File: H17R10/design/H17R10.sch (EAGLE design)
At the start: 94 parts, among them P1 HEXABIT__X3_NO_P1_P2_P3_P4_P5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, P4 PAD4, P5 PAD4, P6 PAD4, U1 STM32F091RBT6STMICROELECTRONI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, U2 POWERSTEP01, U3 TEXAS_INSTRUMENTS_ISO7741DBQR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, U4 TEXAS_INSTRUMENTS_ISO7742DBQR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, X1 XTALL_CSTCE8M00G52

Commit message: -Changing the MCU to STM32G0B1CEU6N -Editing the electronic design -Editing the layout design to improve the performance
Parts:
- removed A1, A2, B1, B2, BZY: YELLOW, HEXABITZ_USER_INTERFACE_PARTS:VLMY1300-GS08
- removed B, C, D, R: PAD1, Hexabitz:PAD1
- removed C22: 1.00uF, Hexabitz:C-0805-POL
- removed C23, C24: 4.7uF, Hexabitz:C-0805-POL
- removed C25: 10nF, Hexabitz:C-0603
- removed C26, C27, C28, C29: 100nF, Hexabitz:C-0603
- removed CCW, CW, PWR: Green, HEXABITZ_USER_INTERFACE_PARTS:VLMTG1300-GS08
- removed D0, FLT, S: RED, HEXABITZ_USER_INTERFACE_PARTS:VLMS1300-GS08
- removed EMG_SW, SPI_MTR: 3-644456-2, HEXABITZ_USER_INTERFACE_PARTS:3-644456-2
- removed P1: HEXABIT__X3_NO_P1_P2_P3_P4_P5_P6_P11_P12, hexabitz_connectors:HEXABIT__X3_NO_P1_P2_P3_P4_P5_P6_P11_P12
- removed P4, P5, P6, VCCIO, VCCIO1, VS: PAD4, HEXABITZ_CONNECTION_PARTS:PAD4
- removed R16, R17, R18, R19: 10k, HEXABITZ_RCLS:R-0805
- removed R20, R21: 330, HEXABITZ_RCLS:R-0603
- removed R22, R27, R33, R34: DNP, HEXABITZ_RCLS:R-0603
- removed R23: 0R, HEXABITZ_RCLS:R-0603
- removed R24, R28: DNP, HEXABITZ_RCLS:R-0805
- removed R25, R26: 39K, HEXABITZ_RCLS:R-0603
- removed R31: 270.0R, HEXABITZ_RCLS:R-0603
- removed R32: 10.0K, Hexabitz:R-0603
- removed U3: TEXAS_INSTRUMENTS_ISO7741DBQRTEXAS_INSTRUMENTS_ISO7741DBQR_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, HEXABITZ_ICs:TEXAS_INSTRUMENTS_ISO7741DBQRTEXAS_INSTRUMENTS_ISO7741DBQR_0_0
- removed U4: TEXAS_INSTRUMENTS_ISO7742DBQRTEXAS_INSTRUMENTS_ISO7742DBQR_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, Texas Instruments - ISO7742DBQR:TEXAS_INSTRUMENTS_ISO7742DBQRTEXAS_INSTRUMENTS_ISO7742DBQR_0_3
- added C20: 470nF, HEXABITZ_RCLS:C-0603
- added CK, CS, SDI, SDO: PAD4, HEXABITZ_CONNECTION_PARTS:PAD4
- added D2: STMICROELECTRONICS_BAT46ZFILMSTMICROELECTRONICS_BAT46ZFILM_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, HEXABITZ_RCLS:STMICROELECTRONICS_BAT46ZFILMSTMICROELECTRONICS_BAT46ZFILM_0_3
- added D3, D5, D6, D7: YELLOW, HEXABITZ_USER_INTERFACE_PARTS:VLMY1300-GS08
- added D4: STMICROELECTRONICS_BAR43SFILMSTMICROELECTRONICS_BAR43SFILM_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, HEXABITZ_RCLS:STMICROELECTRONICS_BAR43SFILMSTMICROELECTRONICS_BAR43SFILM_0_0
- added D8: RED, HEXABITZ_USER_INTERFACE_PARTS:VLMS1300-GS08
- added FB1: (no value), HEXABITZ_RCLS:FB-TDK_MMZ1608Y300B
- added J1: 3-644456-2, HEXABITZ_USER_INTERFACE_PARTS:3-644456-2
- added JP1: (no value), HEXABITZ_USER_INTERFACE_PARTS:PINHD-1X1
- added JP2: (no value), pinhead:PINHD-1X3
- added R12: 330, HEXABITZ_RCLS:R-0603
- added SJ1, SJ2: (no value), jumper:SJW
- added U$1: HEXABIT_17.32_X3_NO_P1_P2_P3_P4_P5_P6_P11_P12, hexabitz_connectors:HEXABIT_17.32_X3_NO_P1_P2_P3_P4_P5_P6_P11_P12
- C1: MFN TDK CORPORATION -> AVX CORPORATION; MPN C1608X7R1H104K080AA -> 0603YC104K4T2A; OCTOPART_URL https://octopart.com/c1608x7r1h104k080aa-tdk-25947665?r=sp -> 'https://octopart.com/0603yc104k4t2a-avx+interconnect+%2F+e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; TOLERANCE (none) -> 10%; VOLTAGE_RATING (none) -> 16.0 V
- C10: value 220nF -> 68uF; device HEXABITZ_RCLS:C-0805 -> HEXABITZ_RCLS:WCAP-ASLI_12.5X14EEVFK2A680Q
- C14: value 68uF -> 220nF; device HEXABITZ_RCLS:WCAP-ASLI_12.5X14EEVFK2A680Q -> HEXABITZ_RCLS:C-0805
- C15: value 68uF -> 47nF; device HEXABITZ_RCLS:WCAP-ASLI_12.5X14EEVFK2A680Q -> HEXABITZ_RCLS:C-0805; MFN (none) -> KEMET; MPN (none) -> C0805C473K1RACTU; OCTOPART_URL (none) -> https://octopart.com/c0805c473k1ractu-kemet-12557765?r=sp; VOLTAGE_RATING (none) -> 100V
- C16, C17, C6: MFN TDK CORPORATION -> AVX CORPORATION; MPN C1608X7R1H104K080AA -> '0603YC104K4T2A; OCTOPART_URL https://octopart.com/c1608x7r1h104k080aa-tdk-25947665?r=sp -> 'https://octopart.com/0603yc104k4t2a-avx+interconnect+%2F+e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; TOLERANCE (none) -> 10%; VOLTAGE_RATING (none) -> 16.0 V
- C18: value 100nF -> 470nF; CAPACITANCE 100nF -> (none); MFN TDK CORPORATION -> TDK; MPN C1608X7R1H104K080AA -> CGA3E3X7R1E474K080AE; OCTOPART_URL https://octopart.com/c1608x7r1h104k080aa-tdk-25947665?r=sp -> https://octopart.com/search?q=CAP+CER+470nF+25V+X7R+0603&cu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; VOLTAGE_RATING (none) -> 100V
- C19: value 100nF -> 220nF; CAPACITANCE 100nF -> (none); MFN TDK CORPORATION -> TDK; MPN C1608X7R1H104K080AA -> CGA3E3X7R1V224K080AE; OCTOPART_URL https://octopart.com/c1608x7r1h104k080aa-tdk-25947665?r=sp -> https://octopart.com/cga3e3x7r1v224k080ae-tdk-68305867?r=sp
- C2: value 220nF -> 100nF; CAPACITANCE (none) -> 100nF; MFN TDK -> AVX CORPORATION; MPN CGA3E3X7R1V224K080AE -> '0603YC104K4T2A; OCTOPART_URL https://octopart.com/cga3e3x7r1v224k080ae-tdk-68305867?r=sp -> 'https://octopart.com/0603yc104k4t2a-avx+interconnect+%2F+e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; TOLERANCE (none) -> 10%; VOLTAGE_RATING (none) -> 16.0 V
- C21: value 100nF -> 22uF; device HEXABITZ_RCLS:C-0603 -> HEXABITZ_RCLS:C-0805-POL; CAPACITANCE 100nF -> (none); MPN C0603C104K8RACTU -> T491A226K006AT; OCTOPART_URL https://octopart.com/c0603c104k8ractu-kemet-145075?r=sp&s=9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 -> https://octopart.com/t491a226k006at-kemet-968601?r=sp; TOLERANCE 10% -> (none); VOLTAGE_RATING 10V -> 6.3V
- C3: value 470nF -> 4.7uF; device HEXABITZ_RCLS:C-0603 -> HEXABITZ_RCLS:C-0805-POL; CAPACITANCE (none) -> 4.7uF; MFN TDK -> 'Panasonic; MPN CGA3E3X7R1E474K080AE -> '10TPU4R7MSI; OCTOPART_URL https://octopart.com/search?q=CAP+CER+470nF+25V+X7R+0603&cu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 -> https://octopart.com/10tpu4r7msi-panasonic-29487748?r=sp; TOLERANCE (none) -> 20%; VOLTAGE_RATING (none) -> 10.0 V
- C4: value 3.3nF -> 100nF; MFN TDK CORPORATION -> AVX CORPORATION; MPN C1608X7R1H104K080AA -> '0603YC104K4T2A; OCTOPART_URL https://octopart.com/c1608x7r1h104k080aa-tdk-25947665?r=sp -> 'https://octopart.com/0603yc104k4t2a-avx+interconnect+%2F+e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; TOLERANCE (none) -> 10%; VOLTAGE_RATING (none) -> 16.0 V
- C5: value DNP -> 1uF; device HEXABITZ_RCLS:C-0603 -> HEXABITZ_RCLS:C-0805-POL; CAPACITANCE (none) -> 4.7uF; MFN (none) -> 'YAGEO [VA]; MPN (none) -> 'CC0805KKX7R7BB105; OCTOPART_URL (none) -> 'https://octopart.com/cc0805kkx7r7bb105-yageo-8376555?r=sp; TOLERANCE (none) -> 20%; VOLTAGE_RATING (none) -> 10.0 V
- C7: value 470nF -> 4.7uF; device HEXABITZ_RCLS:C-0603 -> HEXABITZ_RCLS:C-0805-POL; CAPACITANCE (none) -> 1.00uF; MFN TDK -> 'Panasonic; MPN CGA3E3X7R1E474K080AE -> '10TPU4R7MSI; OCTOPART_URL https://octopart.com/search?q=CAP+CER+470nF+25V+X7R+0603&cu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 -> https://octopart.com/10tpu4r7msi-panasonic-29487748?r=sp; TOLERANCE (none) -> 10%; VOLTAGE_RATING (none) -> 16.0 V
- C8: value 47nF -> 100nF; device HEXABITZ_RCLS:C-0805 -> HEXABITZ_RCLS:C-0603; CAPACITANCE (none) -> 100nF; MFN KEMET -> TDK CORPORATION; MPN C0805C473K1RACTU -> C1608X7R1H104K080AA; OCTOPART_URL https://octopart.com/c0805c473k1ractu-kemet-12557765?r=sp -> https://octopart.com/c1608x7r1h104k080aa-tdk-25947665?r=sp; VOLTAGE_RATING 100V -> (none)
- C9: value 22uF -> 68uF; device HEXABITZ_RCLS:C-0805-POL -> HEXABITZ_RCLS:WCAP-ASLI_12.5X14EEVFK2A680Q; MFN KEMET -> (none); MPN T491A226K006AT -> (none); OCTOPART_URL https://octopart.com/t491a226k006at-kemet-968601?r=sp -> (none); VOLTAGE_RATING 6.3V -> (none)
- D1: value STMICROELECTRONICS_BAR43SFILMSTMICROELECTRONICS_BAR43SFILM_0_0 -> RED; device HEXABITZ_RCLS:STMICROELECTRONICS_BAR43SFILMSTMICROELECTRONICS_BAR43SFILM_0_0 -> HEXABITZ_USER_INTERFACE_PARTS:VLMS1300-GS08
- D10: value STMICROELECTRONICS_BAT46ZFILMSTMICROELECTRONICS_BAT46ZFILM_0_3 -> YELLOW; device HEXABITZ_RCLS:STMICROELECTRONICS_BAT46ZFILMSTMICROELECTRONICS_BAT46ZFILM_0_3 -> HEXABITZ_USER_INTERFACE_PARTS:VLMY1300-GS08; MFN (none) -> Lite-On; MPN (none) -> LTST-C170YKT; OCTOPART_URL (none) -> https://octopart.com/ltst-c170ykt-lite-on-549813?r=sp
- D9: value STMICROELECTRONICS_BAT46ZFILMSTMICROELECTRONICS_BAT46ZFILM_0_3 -> Green; device HEXABITZ_RCLS:STMICROELECTRONICS_BAT46ZFILMSTMICROELECTRONICS_BAT46ZFILM_0_3 -> HEXABITZ_USER_INTERFACE_PARTS:VLMTG1300-GS08; MFN (none) -> Lite-On; MPN (none) -> LTST-C170GKT; OCTOPART_URL (none) -> https://octopart.com/ltst-c170gkt-lite-on-549817?r=sp
- R1: value 0R1 -> 0.0R; device HEXABITZ_RCLS:R-US_R2512 -> HEXABITZ_RCLS:R-0603; MFN Yageo -> YAGEO [VR]; MPN PE2512FKE7W0R1L -> RC0603JR-070RL; OCTOPART_URL https://octopart.com/pe2512fke7w0r1l-yageo-71384148?r=sp -> https://octopart.com/rc0603jr-070rl-yageo-1241539?r=sp; RESISTANCE (none) -> 0R
- R10, R9: value 270.0R -> 10k; device HEXABITZ_RCLS:R-0603 -> HEXABITZ_RCLS:R-0805; MFN Yageo -> Panasonic; MPN RC0603FR-07270RL -> ERJ-6GEYJ103V; OCTOPART_URL https://octopart.com/search?q=RC0603FR-07270RL&start=0 -> https://octopart.com/erj-6geyj103v-panasonic-55422885?r=sp; RESISTANCE 270.0 Ohm -> (none); TOLERANCE 1% -> (none)
- R11: value 270.0R -> 330; MPN RC0603FR-07270RL -> RC0603JR-07330RL; OCTOPART_URL https://octopart.com/search?q=RC0603FR-07270RL&start=0 -> https://octopart.com/rc0603jr-07330rl-yageo-39803615?r=sp; RESISTANCE 270.0 Ohm -> 330; TOLERANCE 1% -> (none)
- R14: value 330 -> 39K; MPN RC0603JR-07330RL -> RC0603FR-0739KL; OCTOPART_URL https://octopart.com/rc0603jr-07330rl-yageo-39803615?r=sp -> https://octopart.com/rc0603fr-0739kl-yageo-55402883?r=sp; RESISTANCE 330 -> 39K
- R15: value 0R -> 330; MPN RC0603JR-070RL -> RC0603JR-07330RL; OCTOPART_URL https://octopart.com/rc0603jr-070rl-yageo-1241539?r=sp -> https://octopart.com/rc0603jr-07330rl-yageo-39803615?r=sp; RESISTANCE (none) -> 330
- R2: value 0R1 -> 270R; device HEXABITZ_RCLS:R-US_R2512 -> HEXABITZ_RCLS:R-0603; MFN Yageo -> 'Panasonic; MPN PE2512FKE7W0R1L -> 'ERJ-3GEYJ271V; OCTOPART_URL https://octopart.com/pe2512fke7w0r1l-yageo-71384148?r=sp -> https://octopart.com/erj-3geyj271v-panasonic-55560546?r=sp; RESISTANCE (none) -> 270R
- R3: value 0R -> 10K; DESCRIPTION RC Series 0603 0.1 W 0 Ohm Jumper Surface Mount Thick Film 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 -> (none); MFN Yageo -> Vishay; MPN RC0603JR-070RL -> '060300J0103T5E; OCTOPART_URL https://octopart.com/rc0603jr-070rl-yageo-1241539?r=sp -> https://octopart.com/search?q=060300J0103T5E&currency=USD&s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; RESISTANCE (none) -> 10K
- R4, R6: value DNP -> 0R1; device HEXABITZ_RCLS:R-0603 -> HEXABITZ_RCLS:R-US_R2512; MFN (none) -> Yageo; MPN DNP -> PE2512FKE7W0R1L; OCTOPART_URL (none) -> https://octopart.com/pe2512fke7w0r1l-yageo-71384148?r=sp
- R5: value DNP -> 39K; MFN (none) -> Yageo; MPN DNP -> RC0603FR-0739KL; OCTOPART_URL (none) -> https://octopart.com/rc0603fr-0739kl-yageo-55402883?r=sp; RESISTANCE (none) -> 39K
- R7: value DNP -> 10k; device HEXABITZ_RCLS:R-0603 -> HEXABITZ_RCLS:R-0805; MFN (none) -> Panasonic; MPN DNP -> ERJ-6GEYJ103V; OCTOPART_URL (none) -> https://octopart.com/erj-6geyj103v-panasonic-55422885?r=sp
- R8: value 0R -> 10k; device HEXABITZ_RCLS:R-0603 -> HEXABITZ_RCLS:R-0805; DESCRIPTION RC Series 0603 0.1 W 0 Ohm Jumper Surface Mount Thick Film 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 -> (none); MFN Yageo -> Panasonic; MPN RC0603JR-070RL -> ERJ-6GEYJ103V; OCTOPART_URL https://octopart.com/rc0603jr-070rl-yageo-1241539?r=sp -> https://octopart.com/erj-6geyj103v-panasonic-55422885?r=sp
- U1: value STM32F091RBT6STMICROELECTRONICS_STM32F091RBT6_0_1 -> STM32G0B1CEU6NUFQFPN48_STM32_STM; device Hexabitz:STM32F091RBT6STMICROELECTRONICS_STM32F091RBT6_0_1 -> HEXABITZ_ICs:STM32G0B1CEU6NUFQFPN48_STM32_STM; MFN STMicroelectronics -> (none); OCTOPART_URL https://octopart.com/stm32f091rbt6-stmicroelectronics-51988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 -> https://octopart.com/stm32g0b1ceu6n-stmicroelectronics-1163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
- U2: device HEXABITZ_ICs:POWERSTEP01 -> POWERSTEP01:POWERSTEP01
- X1: value XTALL_CSTCE8M00G52 -> 8MHZ; device Hexabitz:XTALL_CSTCE8M00G52 -> HEXABITZ_OTHER_PARTS:XTALL_CSTCE8M00G52; MPN (none) -> CSTNE8M00G550000R0; OCTOPART_URL (none) -> https://octopart.com/cstne8m00g550000r0-murata-91406934?r=sp
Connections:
- removed net ADC_IN: C5.1, R27.2, R28.1, U2B.ADCIN
- removed net B1: B.P$1, R32.2, U1.PF11-BOOT0
- removed net CK: U2A.CK, U3.OUTB
- removed net CP: C8.1, U2B.CP
- removed net FORWARD: R10.2, U1.PB12
- removed net GND1: A1.C, A2.C, B1.C, B2.C, C1.2, C10.2, C11.2, C12.2, C13.2, C14.-, C15.-, C16.2, C18.2, C2.2, C4.2, C5.2, C6.2, C7.2, C9.-, EMG_SW.2, P6.P$1, PWR.C, R1.1, R2.1, R27.1, U2A.GND, U2A.GND_2, U2B.GND, U2B.GND_2, U3.1_GND2, U3.2_GND2, U4.1_GND2, U4.2_GND2, X2-2.KL
- removed net MC_BUSY/SYNC: U1.PC5, U4.INA
- removed net MC_CK: U1.PB3, U3.INB
- removed net MC_CS: U1.PB6, U3.INA
- removed net MC_FLAG: U1.PC4, U4.INB
- removed net MC_MISO: R33.1, U1.PB4, U3.OUTD
- removed net MC_MOSI: R34.1, U1.PB5, U3.INC
- removed net MC_STBY/RESET: U1.PA6, U4.OUTD
- removed net MS_STCK: U1.PA7, U4.OUTC
- removed net N$11: R9.1, S.A
- removed net N$18: R3.1, U3.OUTC
- removed net N$20: R4.1, R6.1, SPI_MTR.2
- removed net N$21: R5.1, R7.1, SPI_MTR.1
- removed net N$22: R22.2, U2B.OSCOUT
- removed net N$23: R22.1, U2B.OSCIN
- removed net N$24: CCW.A, R10.1
- removed net N$25: CW.A, R11.1
- removed net N$3: R31.2, U1.PA8
- removed net N$7: D.P$1, U1.PA13
- removed net N$8: C7.1, D9.CATHODE, R24.1, U2B.VCC
- removed net N$9: C.P$1, U1.PA14
- removed net R1: C21.1, R.P$1, U1.NRST
- removed net REVERSED: R11.2, U1.PA12
- removed net SENSE_A: R2.2, U2A.SENSEA1_P, U2A.SENSEA1_P_2, U2A.SENSEA1_P_3, U2A.SENSEA2_P, U2A.SENSEA2_P_2, U2A.SENSEA2_P_3, U2A.SENSEA_S, U2B.SENSEA1_P, U2B.SENSEA2_P
- removed net SENSE_B: R1.2, U2A.SENSEB_S, U2B.SENSEB1_P, U2B.SENSEB1_P_2, U2B.SENSEB1_P_3, U2B.SENSEB1_P_4, U2B.SENSEB2_P, U2B.SENSEB2_P_2, U2B.SENSEB2_P_3, U2B.SENSEB2_P_4
- removed net STBY/RESET: C6.1, U2A.!STBY/!RESET, U4.IND
- removed net STOPPED: R9.2, U1.PA11
- removed net UART1_RX*: P1.SD9, U1.PA10
- removed net UART1_TX*: P1.SU9, U1.PA9
- removed net UART2_RX*: P1.SD7, U1.PA3
- removed net UART2_TX*: P1.SU7, U1.PA2
- removed net UART3_RX: U1.PB11
- removed net UART3_TX: U1.PB10
- removed net UART4_RX: P1.SD10, U1.PC11
- removed net UART4_TX: P1.SU10, U1.PC10
- removed net UART6_RX: P1.SD8, U1.PA5
- removed net UART6_TX: P1.SU8, U1.PA4
- removed net UART7_RX: U1.PC1
- removed net UART7_TX: U1.PC0
- removed net UART8_RX: U1.PC3
- removed net UART8_TX: U1.PC2
- removed net VCCIO: C1.1, C16.1, C18.1, C4.1, R13.2, R14.2, R15.1, R21.2, R25.2, R26.2, U2A.VDDIO, U3.EN2, U3.VCC2, U4.EN2, U4.VCC2, VCCIO.P$1, VCCIO1.P$1
- removed net VSREG: D10.ANODE, R23.2, R24.2, U2B.VSREG
- removed net VSS: C10.1, C11.1, C12.1, C13.1, C14.+, C15.+, C3.2, D1.A2, D10.CATHODE, R23.1, R28.2, U2A.VS, U2A.VS_10, U2A.VS_11, U2A.VS_12, U2A.VS_13, U2A.VS_14, U2A.VS_15, U2A.VS_16, U2A.VS_17, U2A.VS_18, U2A.VS_19, U2A.VS_2, U2A.VS_20, U2A.VS_21, U2A.VS_22, U2A.VS_23, U2A.VS_24, U2A.VS_25, U2A.VS_3, U2A.VS_4, U2A.VS_5, U2A.VS_6, U2A.VS_7, U2A.VS_8, U2A.VS_9, U2B.VS, U2B.VS_10, U2B.VS_11, U2B.VS_12, U2B.VS_13, U2B.VS_14, U2B.VS_15, U2B.VS_16, U2B.VS_17, U2B.VS_18, U2B.VS_19, U2B.VS_2, U2B.VS_20, U2B.VS_3, U2B.VS_4, U2B.VS_5, U2B.VS_6, U2B.VS_7, U2B.VS_8, U2B.VS_9, VS.P$1, X2-1.KL
- removed net V_BOOT: C3.1, D1.K1, U2B.VBOOT
- new net C: JP2.1, JP2.2, R3.2, U1.PA14-BOOT0
- new net D: JP2.3, U1.PA13
- new net N$26: C18.2, D4.K1, U2.VBOOT
- new net N$27: C20.1, D2.CATHODE, U2.VCC
- new net N$32: C15.2, D4.A1/K2
- new net RESET: C8.1, U2.!STBY!/!RESET
- new net SCK: CK.P$1, U1.PB3, U2.CK
- new net SENSEA: R4.2, SJ1.2, U2.SENSEA_P, U2.SENSEA_S
- new net SENSEB: R6.2, SJ2.2, U2.SENSEB_P, U2.SENSEB_S
- new net USART2_RX: U$1.SD8, U1.PA3
- new net USART2_TX: U$1.SU8, U1.PA2
- new net USART3_RX: U$1.SD9, U1.PB11
- new net USART3_TX: U$1.SU9, U1.PB10
- new net USART5_RX: U$1.SD10, U1.PD2
- new net USART5_TX: U$1.SU10, U1.PD3
- new net USART6_RX: U$1.SD7, U1.PB9
- new net USART6_TX: U$1.SU7, U1.PB8
- new net VDDA: C16.2, C17.2, C19.1, C2.2, C21.+, C3.+, C4.2, C5.+, D2.ANODE, FB1.2, R11.2, R12.2, R13.2, R14.2, R15.2, R5.2, U1.VBAT, U1.VDD/VDDA, U1.VREF+, U2.VCCREG, U2.VDDIO, U2.VREG
- new net VS: C10.+, C11.1, C12.1, C13.1, C14.1, C18.1, C9.+, D4.A2, U2.VS, U2.VSREG, X2-1.KL
- new net VSSA: C10.-, C11.2, C12.2, C13.2, C14.2, C16.1, C17.1, C19.2, C2.1, C20.2, C21.-, C3.-, C4.1, C5.-, C8.2, C9.-, D3.C, D5.C, D6.C, D7.C, D9.C, J1.2, R1.2, R4.1, R6.1, SJ1.1, SJ2.1, U1.VSS/VSSA, U2.GND, X2-2.KL
- net BUSY/SYNC: now also D10.C, R14.1, U2.!BUSY!/SYNC; no longer BZY.C, R26.1, U2A.!BUSY/SYNC, U4.OUTA
- net CS: now also CS.P$1, U1.PA15, U2.!CS; no longer U2A.!CS, U3.OUTA
- net FLAG: now also D8.C, U2.!FLAG; no longer FLT.C, U2A.!FLAG, U4.OUTB
- net GND: now also C1.1, C6.1, C7.-, D1.C, R1.1, R3.1, U$1.GND7, U$1.GND8, U$1.GND9, U1.EPAD, U1.VSS; no longer C17.2, C19.2, C21.2, C22.-, C23.-, C24.-, C25.2, C26.2, C27.2, C28.2, C29.2, CCW.C, CW.C, D0.C, P1.GND7, P1.GND8, P1.GND9, P5.P$1, R32.1, S.C, U1.1_VSS, U1.2_VSS, U1.3_VSS, U1.4_VSS, U1.PC12, U1.PD2, U1.VSSA, U3.1_GND1, U3.2_GND1, U4.1_GND1, U4.2_GND1
- net N$1: now also U1.PF0-OSC_IN, X1.1; no longer C2.1, C9.+, D9.ANODE, R15.2, R20.2, U2B.VCCREG, U2B.VREG
- net N$10: now also D3.A, R7.1; no longer A1.A, R16.1
- net N$12: now also C1.2, JP1.1, U1.PF2-NRST; no longer BZY.A, R14.1
- net N$13: now also D8.A, R11.1; no longer FLT.A, R21.1
- net N$14: now also D9.A, R12.1; no longer PWR.A, R20.1
- net N$15: now also D5.A, R8.1; no longer A2.A, R17.1
- net N$16: now also D6.A, R9.1; no longer B1.A, R18.1
- net N$17: now also R2.2, U1.PB14; no longer B2.A, R19.1
- net N$19: now also D1.A, R2.1; no longer R8.1, U3.IND
- net N$2: now also U1.PF1-OSC_OUT, X1.3; no longer C8.2, D1.A1/K2
- net N$4: now also C15.1, U2.CP; no longer D0.A, R31.1
- net N$5: now also D10.A, R15.1; no longer U1.PF0-OSC_IN(PF0), X1.1
- net N$6: now also D7.A, R10.1; no longer U1.PF1-OSC_OUT(PF1), X1.3
- net OUTA1: now also R10.2, U2.OUTA1; no longer R16.2, U2A.OUTA1, U2A.OUTA1_2, U2B.OUTA1, U2B.OUTA1_2
- net OUTA2: now also R9.2, U2.OUTA2; no longer R17.2, U2A.OUTA2, U2A.OUTA2_2, U2A.OUTA2_3, U2B.OUTA2
- net OUTB1: now also R8.2, U2.OUTB1; no longer R18.2, U2B.OUTB1, U2B.OUTB1_2, U2B.OUTB1_3, U2B.OUTB1_4
- net OUTB2: now also R7.2, U2.OUTB2; no longer R19.2, U2A.OUTB2, U2B.OUTB2, U2B.OUTB2_2, U2B.OUTB2_3
- net SDI: now also SDI.P$1, U1.PB5, U2.SDI; no longer R3.2, R4.2, R5.2, U2A.SDI
- net SDO: now also SDO.P$1, U1.PB4, U2.SDO; no longer R6.2, R7.2, R8.2, U2A.SDO
- net STCK: now also R5.1, U2.STCK; no longer R25.1, U2A.STCK, U4.INC
- net SW: now also J1.1, U2.SW; no longer EMG_SW.1, U2A.SW
- net VDD: now also C6.2, C7.+, FB1.1, U$1.VDD7, U$1.VDD8, U$1.VDD9; no longer C17.1, C19.1, C22.+, C23.+, C24.+, C25.1, C26.1, C27.1, C28.1, C29.1, P1.VDD7, P1.VDD8, P1.VDD9, P4.P$1, R33.2, R34.2, U1.1_VDD, U1.2_VDD, U1.3_VDD, U1.VBAT, U1.VDDA, U3.EN1, U3.VCC1, U4.EN1, U4.VCC1
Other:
- note added: "B"
- note added: "H17R10_Backened"
- note added: "H17R10_Frontened"
- note added: "Ibrahim Zaeiter"
- note added: "R"
- note added: "SPI1 ,SPI3"
- note added: "Stepper motor driver 10A(RMS) , 10.5 to 85V"
- note added: "VDD\\\VDDA Coupling"
- note added: "VS = (10.5 V - 85 V)"
- note added: "Vref Coupling"
- note removed: "Amir Tabbakh"
- note removed: "BOOT STRAP"
- note removed: "C:/Users/Admin/Desktop/logodraft.bmp"
- note removed: "Control pins"
- note removed: "GND is isolated"
- note removed: "H17R10_Backend"
- note removed: "H17R10_Frontend_1"
- note removed: "H17R10_Frontend_2"
- note removed: "H17R10_Frontend_3"
- note removed: "POWER WITH 80v MAX PULL 10A RMS MAX"
- note removed: "SPI"
- note removed: "VBAT"
- note removed: "VDD = +3.3V"
- note removed: "VDD Coupling"
- note removed: "VDDA Coupling"
- note removed: "Vccio = 3.3v (output)"
- note removed: "Vs=80v max"
- note removed: "high_power"
- note removed: "isolated Stepper motor driver 10A , 10.5 to 80V"
- note removed: "logic"

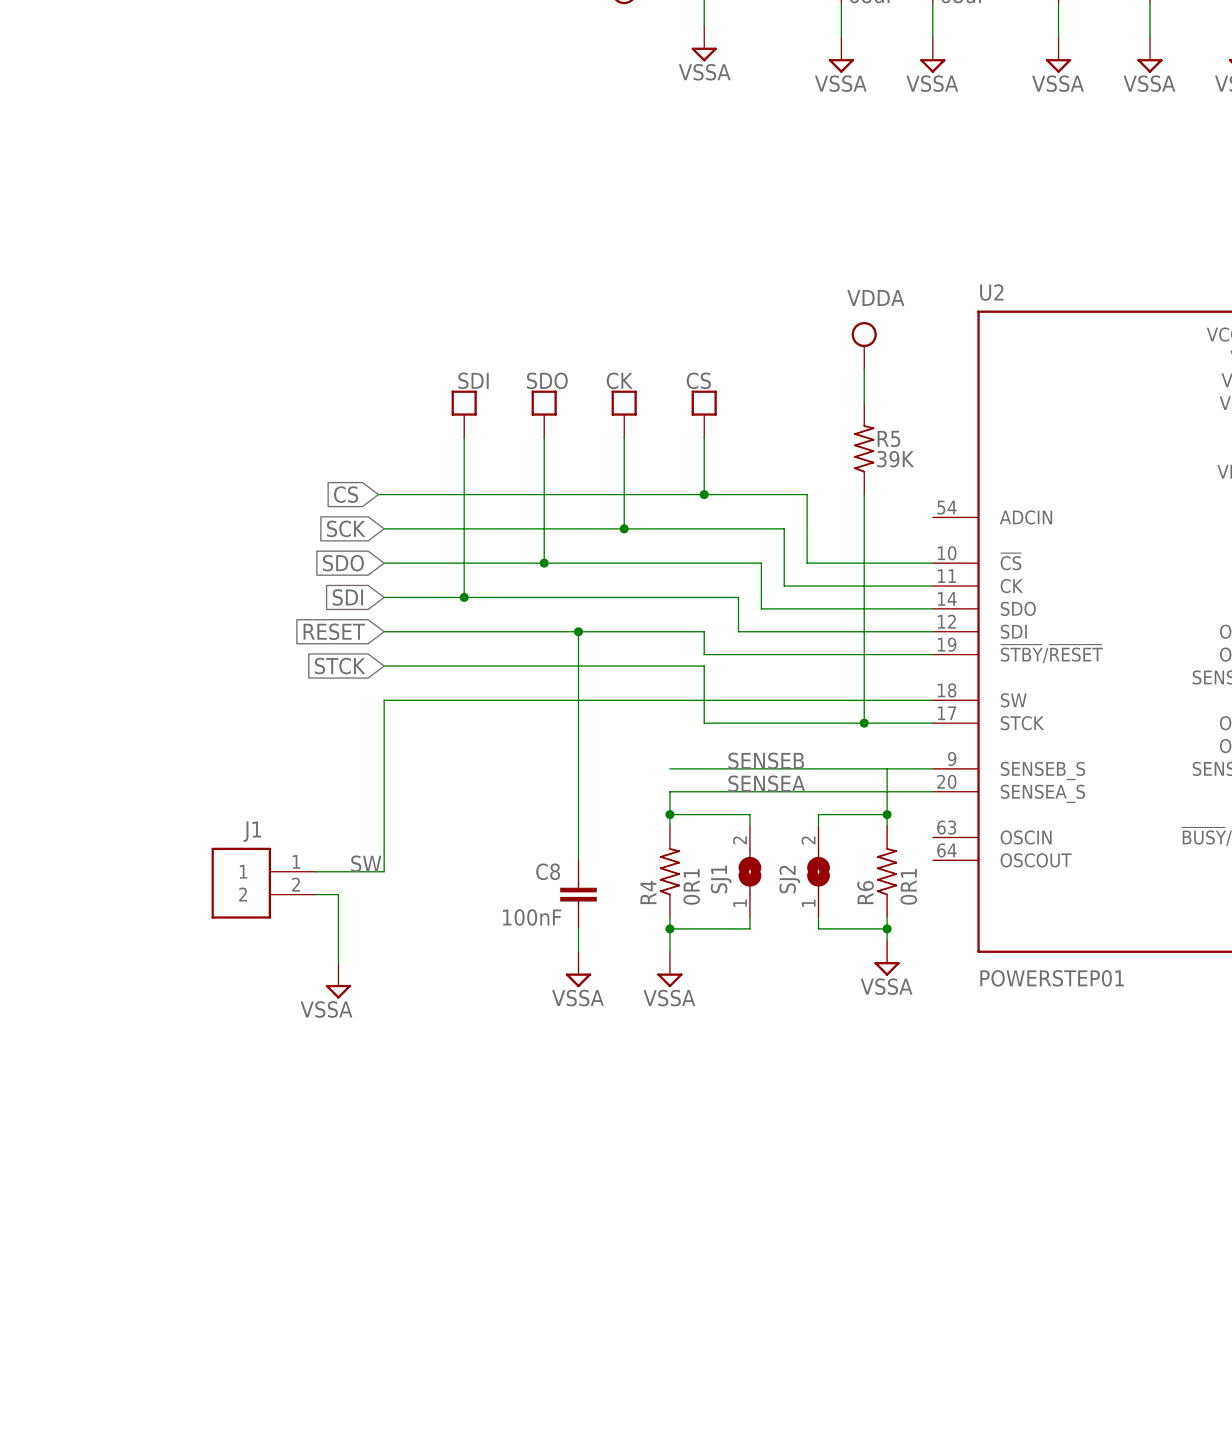
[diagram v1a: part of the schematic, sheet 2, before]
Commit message: -Adding some components to the design to improve the performance
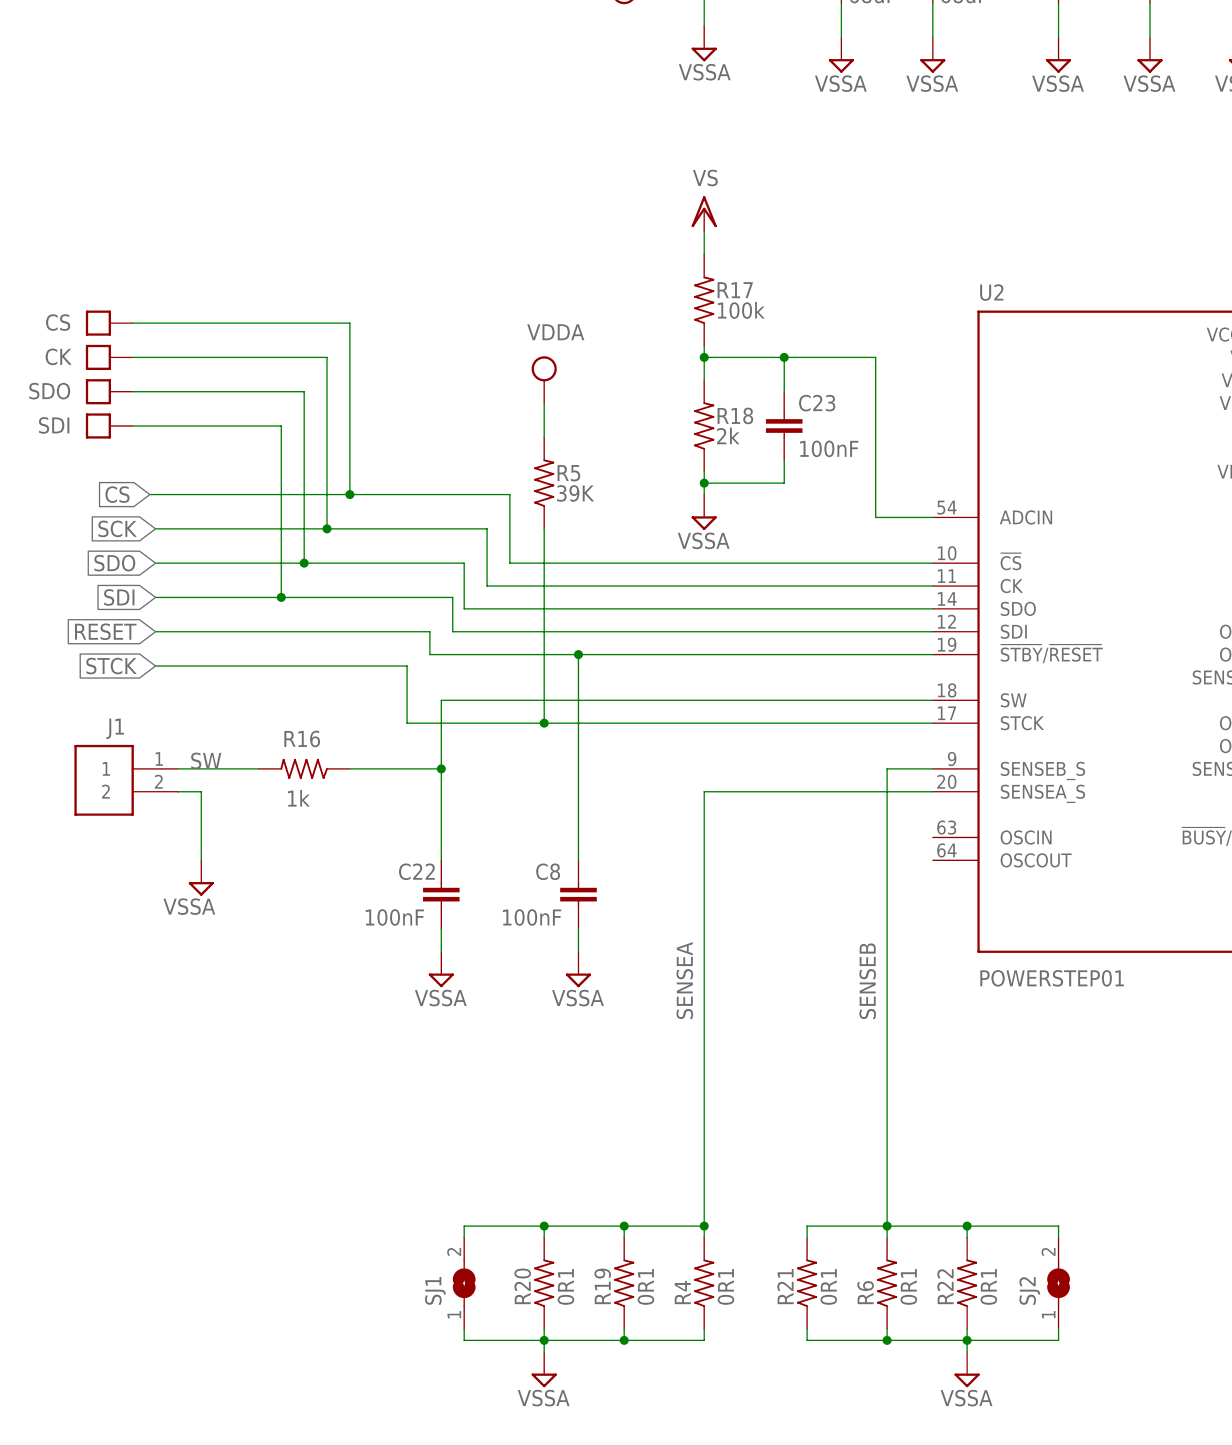
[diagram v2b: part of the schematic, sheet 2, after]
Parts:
- added C22, C23: 100nF, HEXABITZ_RCLS:C-0603
- added R16: 1k, HEXABITZ_RCLS:R-0603
- added R17: 100k, HEXABITZ_RCLS:R-0603
- added R18: 2k, HEXABITZ_RCLS:R-0603
- added R19, R20, R21, R22: 0R1, HEXABITZ_RCLS:R-US_R2512
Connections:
- new net N$3: C22.1, R16.1, U2.SW
- new net N$7: C23.1, R17.1, R18.2, U2.ADCIN
- net SENSEA: now also R19.2, R20.2
- net SENSEB: now also R21.2, R22.2
- net SW: now also R16.2; no longer U2.SW
- net VS: now also R17.2
- net VSSA: now also C22.2, C23.2, R18.1, R19.1, R20.1, R21.1, R22.1
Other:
- moved on the sheet: CK, CS, J1, R4, R5, R6, SDI, SDO, SJ1, SJ2
